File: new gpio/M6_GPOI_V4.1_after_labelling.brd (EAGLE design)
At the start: 100 x 58.4 mm, 32 parts, among them IC4 LT1161, Q5 16MHz, Q8 16MHz, U3 MCP2515, U4 ATMEGA328P_PDIP, X2 MABC96R

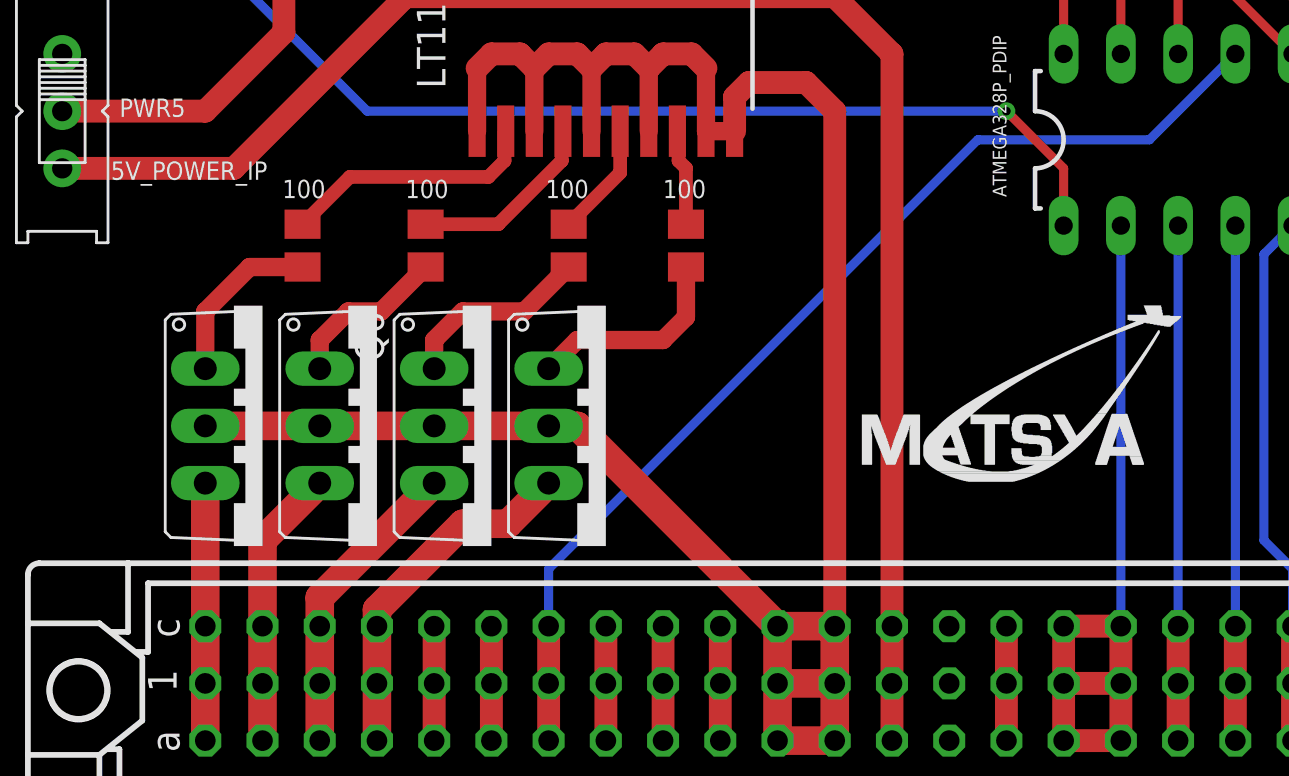
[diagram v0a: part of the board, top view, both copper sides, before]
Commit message: gpio mosfet
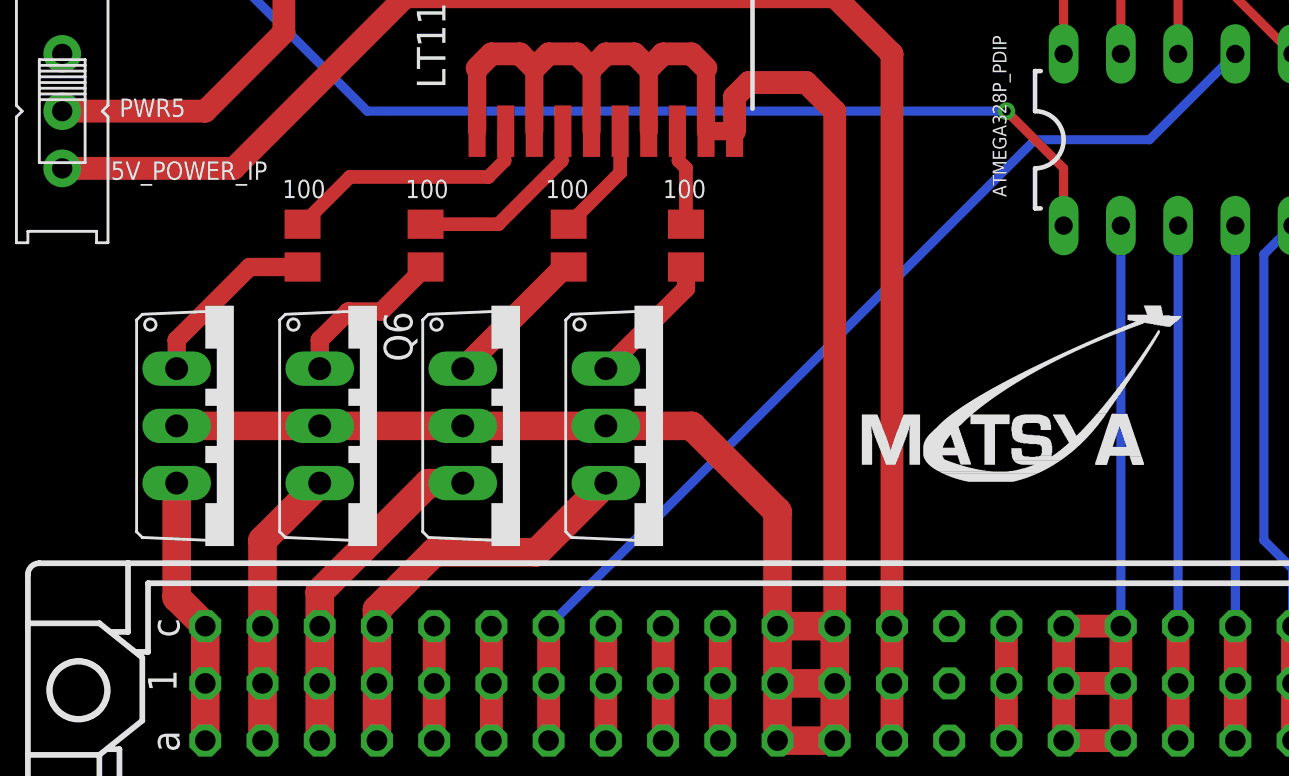
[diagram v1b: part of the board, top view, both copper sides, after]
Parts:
- moved Q9 2.54 mm to (30.5, 19.1)
- moved Q10 1.27 mm to (11.4, 19.1)
- moved Q6 1.27 mm to (24.1, 19.1)
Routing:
- net POWER: track 104.0 -> 108.2 mm
- net PNEU_4_OUT: track 9.27 -> 5.98 mm
- net PNEU_4: track 15.8 -> 18.3 mm
- net PNEU_3_OUT: track 8.58 -> 6.57 mm
- net INT_1: track 47.6 -> 46.1 mm
- net PNEU_3: track 13.5 -> 15.0 mm
- net PNEU_1: track 11.4 -> 12.0 mm
- net PNEU_1_OUT: track 7.67 -> 8.20 mm
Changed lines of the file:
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@@
 <drawing>
 <settings>
-<setting alwaysvectorfont="yes"/>
+<setting alwaysvectorfont="no"/>
 <setting verticaltext="up"/>
 </settings>
@@
 <attribute name="VALUE" x="89.662" y="35.941" size="0.6096" layer="27" font="vector" ratio="20"/>
 </element>
-<element name="Q10" library="adafruit" library_urn="urn:adsk.eagle:library:420" package="TO220V" package3d_urn="urn:adsk.eagle:package:6240882/1" value="" x="12.7" y="19.05" smashed="yes" rot="R270">
-<attribute name="VALUE" x="5.08" y="24.13" size="1.27" layer="27" ratio="10" rot="R270"/>
+<element name="Q10" library="adafruit" library_urn="urn:adsk.eagle:library:420" package="TO220V" package3d_urn="urn:adsk.eagle:package:6240882/1" value="" x="11.43" y="19.05" smashed="yes" rot="R270">
+<attribute name="VALUE" x="3.81" y="24.13" size="1.27" layer="27" ratio="10" rot="R270"/>
 </element>
 <element name="Q5" library="crystal" library_urn="urn:adsk.eagle:library:204" package="HC49/S" package3d_urn="urn:adsk.eagle:package:12071/1" value="16MHz" x="67.31" y="52.578" smashed="yes" rot="R180">
@@
 <attribute name="VALUE" x="72.39" y="56.515" size="1.27" layer="27" ratio="10" rot="R180"/>
 </element>
-<element name="Q6" library="adafruit" library_urn="urn:adsk.eagle:library:420" package="TO220V" package3d_urn="urn:adsk.eagle:package:6240882/1" value="" x="22.86" y="19.05" smashed="yes" rot="R270">
-<attribute name="NAME" x="16.8148" y="24.13" size="1.27" layer="25" ratio="10" rot="R270"/>
-<attribute name="VALUE" x="15.24" y="24.13" size="1.27" layer="27" ratio="10" rot="R270"/>
+<element name="Q6" library="adafruit" library_urn="urn:adsk.eagle:library:420" package="TO220V" package3d_urn="urn:adsk.eagle:package:6240882/1" value="" x="24.13" y="19.05" smashed="yes" rot="R270">
+<attribute name="NAME" x="18.0848" y="24.13" size="1.27" layer="25" ratio="10" rot="R270"/>
+<attribute name="VALUE" x="16.51" y="24.13" size="1.27" layer="27" ratio="10" rot="R270"/>
 </element>
 <element name="Q7" library="adafruit" library_urn="urn:adsk.eagle:library:420" package="TO220V" package3d_urn="urn:adsk.eagle:package:6240882/1" value="" x="17.78" y="19.05" smashed="yes" rot="R270">
@@
 <attribute name="VALUE" x="72.39" y="15.367" size="1.27" layer="25" ratio="10" rot="R180"/>
 </element>
-<element name="Q9" library="adafruit" library_urn="urn:adsk.eagle:library:420" package="TO220V" package3d_urn="urn:adsk.eagle:package:6240882/1" value="" x="27.94" y="19.05" smashed="yes" rot="R270">
-<attribute name="VALUE" x="20.32" y="24.13" size="1.27" layer="27" ratio="10" rot="R270"/>
+<element name="Q9" library="adafruit" library_urn="urn:adsk.eagle:library:420" package="TO220V" package3d_urn="urn:adsk.eagle:package:6240882/1" value="" x="30.48" y="19.05" smashed="yes" rot="R270">
+<attribute name="VALUE" x="22.86" y="24.13" size="1.27" layer="27" ratio="10" rot="R270"/>
 </element>
 <element name="RD1" library="rcl" library_urn="urn:adsk.eagle:library:334" package="M0805" package3d_urn="urn:adsk.eagle:package:23556/2" value="100" x="31.496" y="27.051" smashed="yes" rot="R90">
@@
 <contactref element="U4" pad="25"/>
 <wire x1="55.88" y1="35.56" x2="52.07" y2="31.75" width="0.4064" layer="16"/>
-<wire x1="52.07" y1="31.75" x2="44.45" y2="31.75" width="0.4064" layer="16"/>
-<wire x1="44.45" y1="31.75" x2="25.4" y2="12.7" width="0.4064" layer="16"/>
-<wire x1="25.4" y1="12.7" x2="25.4" y2="10.16" width="0.4064" layer="16"/>
+<wire x1="52.07" y1="31.75" x2="46.99" y2="31.75" width="0.4064" layer="16"/>
+<wire x1="46.99" y1="31.75" x2="25.4" y2="10.16" width="0.4064" layer="16"/>
 <wire x1="25.4" y1="10.16" x2="25.4" y2="7.62" width="1.016" layer="1"/>
 <wire x1="25.4" y1="7.62" x2="25.4" y2="5.08" width="1.016" layer="1"/>
@@
 <contactref element="RI3" pad="1"/>
 <wire x1="14.478" y1="26.101" x2="12.131" y2="26.101" width="0.8128" layer="1"/>
-<wire x1="12.131" y1="26.101" x2="10.16" y2="24.13" width="0.8128" layer="1"/>
-<wire x1="10.16" y1="24.13" x2="10.16" y2="21.59" width="0.8128" layer="1"/>
+<wire x1="12.131" y1="26.101" x2="8.89" y2="22.86" width="0.8128" layer="1"/>
+<wire x1="8.89" y1="22.86" x2="8.89" y2="21.59" width="0.8128" layer="1"/>
 </signal>
 <signal name="PNEU_2_OUT">
@@
 <contactref element="Q6" pad="1"/>
 <contactref element="RI1" pad="1"/>
-<wire x1="20.32" y1="21.59" x2="20.32" y2="22.86" width="0.8128" layer="1"/>
-<wire x1="20.32" y1="22.86" x2="21.59" y2="24.13" width="0.8128" layer="1"/>
-<wire x1="24.318" y1="24.13" x2="26.289" y2="26.101" width="0.8128" layer="1"/>
-<wire x1="21.59" y1="24.13" x2="24.318" y2="24.13" width="0.8128" layer="1"/>
+<wire x1="21.59" y1="21.59" x2="26.101" y2="26.101" width="1.016" layer="1"/>
+<wire x1="26.101" y1="26.101" x2="26.289" y2="26.101" width="1.016" layer="1"/>
 </signal>
 <signal name="PNEU_4_OUT">
 <contactref element="Q9" pad="1"/>
 <contactref element="RD1" pad="1"/>
-<wire x1="25.4" y1="21.59" x2="26.67" y2="22.86" width="0.8128" layer="1"/>
-<wire x1="26.67" y1="22.86" x2="30.48" y2="22.86" width="0.8128" layer="1"/>
-<wire x1="30.48" y1="22.86" x2="31.496" y2="23.876" width="0.8128" layer="1"/>
-<wire x1="31.496" y1="23.876" x2="31.496" y2="26.101" width="0.8128" layer="1"/>
+<wire x1="27.94" y1="21.59" x2="31.496" y2="25.146" width="0.8128" layer="1"/>
+<wire x1="31.496" y1="25.146" x2="31.496" y2="26.101" width="0.8128" layer="1"/>
 </signal>
 <signal name="CUSTOMPIN1_M">
@@
 <contactref element="X2" pad="B12"/>
 <contactref element="X2" pad="A12"/>
-<wire x1="10.16" y1="19.05" x2="15.24" y2="19.05" width="1.27" layer="1"/>
-<wire x1="15.24" y1="19.05" x2="20.32" y2="19.05" width="1.27" layer="1"/>
-<wire x1="20.32" y1="19.05" x2="25.4" y2="19.05" width="1.27" layer="1"/>
-<wire x1="25.4" y1="19.05" x2="26.67" y2="19.05" width="1.27" layer="1"/>
-<wire x1="26.67" y1="19.05" x2="35.56" y2="10.16" width="1.27" layer="1"/>
+<wire x1="8.89" y1="19.05" x2="15.24" y2="19.05" width="1.27" layer="1"/>
+<wire x1="15.24" y1="19.05" x2="21.59" y2="19.05" width="1.27" layer="1"/>
+<wire x1="21.59" y1="19.05" x2="27.94" y2="19.05" width="1.27" layer="1"/>
+<wire x1="27.94" y1="19.05" x2="31.75" y2="19.05" width="1.27" layer="1"/>
+<wire x1="35.56" y1="15.24" x2="31.75" y2="19.05" width="1.27" layer="1"/>
+<wire x1="35.56" y1="15.24" x2="35.56" y2="10.16" width="1.27" layer="1"/>
 <wire x1="35.56" y1="10.16" x2="35.56" y2="7.62" width="1.27" layer="1"/>
 <wire x1="35.56" y1="5.08" x2="35.56" y2="7.62" width="1.27" layer="1"/>
@@
 <contactref element="X2" pad="B3"/>
 <contactref element="X2" pad="C3"/>
-<wire x1="20.32" y1="16.51" x2="15.24" y2="11.43" width="1.27" layer="1"/>
-<wire x1="15.24" y1="11.43" x2="15.24" y2="10.16" width="1.27" layer="1"/>
+<wire x1="21.59" y1="16.51" x2="20.066" y2="16.51" width="1.27" layer="1"/>
+<wire x1="20.066" y1="16.51" x2="15.24" y2="11.684" width="1.27" layer="1"/>
+<wire x1="15.24" y1="11.684" x2="15.24" y2="10.16" width="1.27" layer="1"/>
 <wire x1="15.24" y1="10.16" x2="15.24" y2="7.62" width="1.27" layer="1"/>
 <wire x1="15.24" y1="7.62" x2="15.24" y2="5.08" width="1.27" layer="1"/>
@@
 <contactref element="X2" pad="B1"/>
 <contactref element="X2" pad="C1"/>
-<wire x1="10.16" y1="16.51" x2="10.16" y2="10.16" width="1.27" layer="1"/>
+<wire x1="8.89" y1="16.51" x2="8.89" y2="11.43" width="1.27" layer="1"/>
+<wire x1="8.89" y1="11.43" x2="10.16" y2="10.16" width="1.27" layer="1"/>
 <wire x1="10.16" y1="10.16" x2="10.16" y2="7.62" width="1.27" layer="1"/>
 <wire x1="10.16" y1="7.62" x2="10.16" y2="5.08" width="1.27" layer="1"/>
@@
 <contactref element="X2" pad="C4"/>
 <contactref element="X2" pad="A4"/>
-<wire x1="25.4" y1="16.51" x2="23.5966" y2="14.7066" width="1.27" layer="1"/>
-<wire x1="23.5966" y1="14.7066" x2="21.59" y2="14.7066" width="1.27" layer="1"/>
-<wire x1="21.59" y1="14.7066" x2="17.78" y2="10.8966" width="1.27" layer="1"/>
+<wire x1="27.94" y1="16.51" x2="24.8666" y2="13.4366" width="1.27" layer="1"/>
+<wire x1="24.8666" y1="13.4366" x2="20.32" y2="13.4366" width="1.27" layer="1"/>
+<wire x1="20.32" y1="13.4366" x2="17.78" y2="10.8966" width="1.27" layer="1"/>
 <wire x1="17.78" y1="10.8966" x2="17.78" y2="10.16" width="1.27" layer="1"/>
 <wire x1="17.78" y1="10.16" x2="17.78" y2="7.62" width="1.27" layer="1"/>

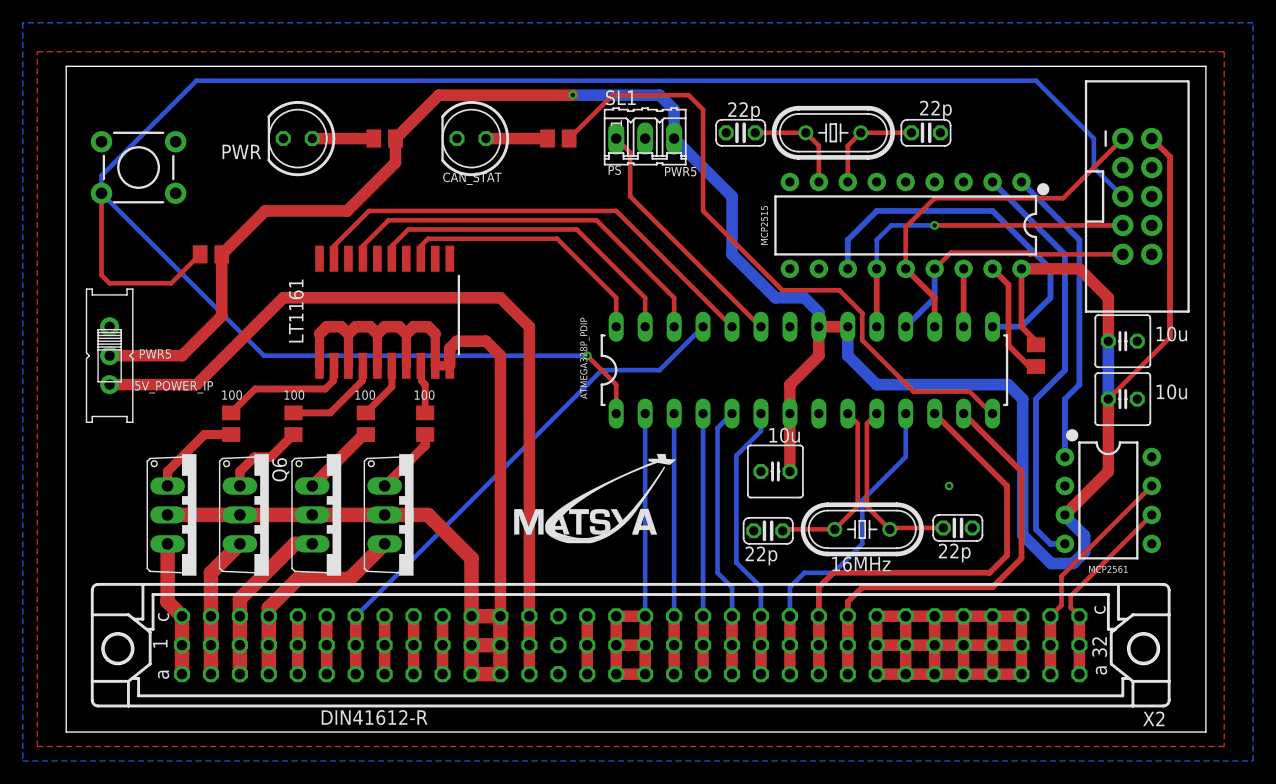
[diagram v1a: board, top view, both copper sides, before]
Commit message: MORE gpio labelling
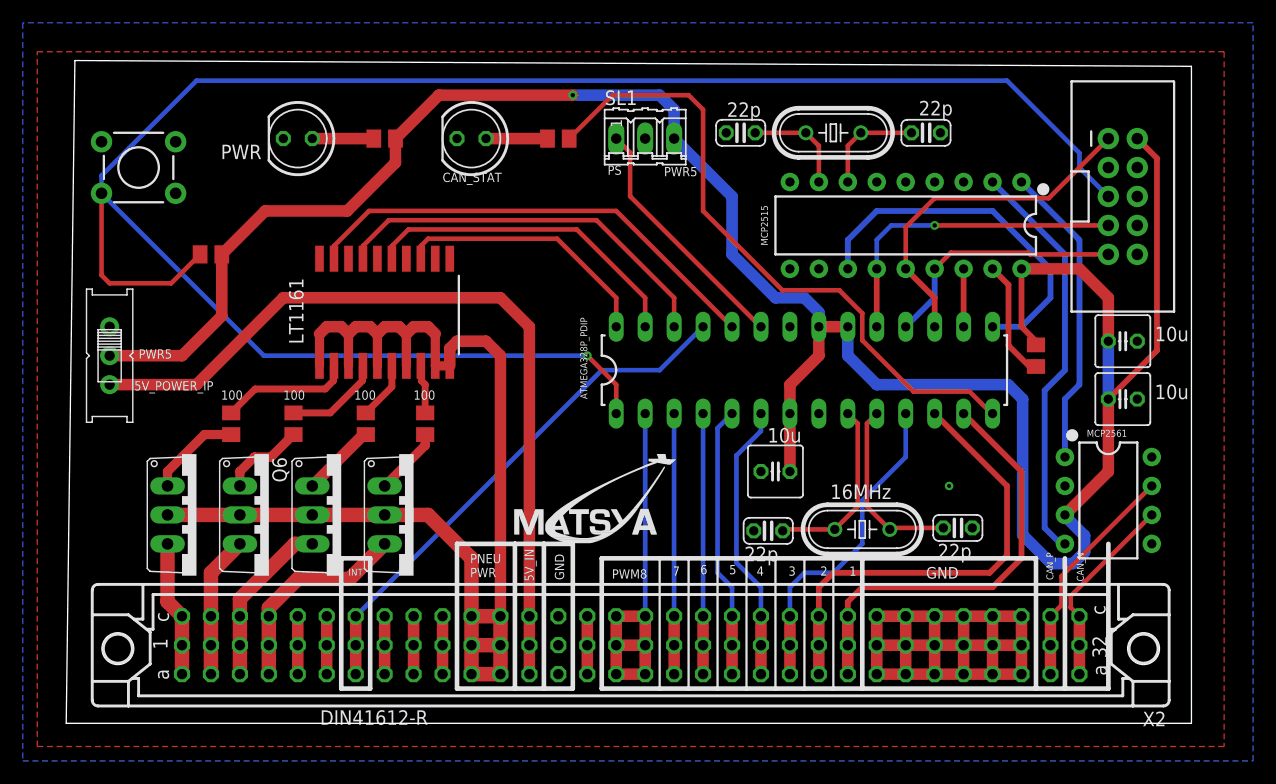
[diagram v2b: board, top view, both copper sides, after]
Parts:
- moved J2 1.27 mm to (92.7, 47.0)
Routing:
- net RESET: track 172.1 -> 170.1 mm
- net CAN_SCK: track 29.7 -> 28.5 mm
- net CAN_MOSI: track 32.1 -> 30.8 mm
- net CAN_MISO: track 23.3 -> 22.0 mm
- net N$7: track 37.2 -> 36.1 mm
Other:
- board size 100 x 58.4 mm -> 98.7 x 58.2 mm
- board text added: "1"
- board text added: "2"
- board text added: "3"
- board text added: "4"
- board text added: "5"
- board text added: "5V_IN"
- board text added: "6"
- board text added: "7"
- board text added: "CAN_N"
- board text added: "CAN_P"
- board text added: "GND"
- board text added: "INT"
- board text added: "PNEU PWR"
- board text added: "PWM8"
